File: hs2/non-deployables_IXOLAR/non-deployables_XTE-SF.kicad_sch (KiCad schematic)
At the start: 9 parts, among them J1 Conn_01x01_Pin

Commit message: setting up prototype arrays
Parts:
- removed SC1, SC2, SC3, SC4, SC5, SC6, SC7, SC8: XTE-SF, solar_cells:xte-sf, symbol Device:XTE-SF
- added D1: 1N5400, Diode_THT:D_DO-201AD_P15.24mm_Horizontal, symbol Diode:1N5400
- added SC1, SC10, SC11, SC12, SC13, SC14, SC15, SC16, SC2, SC3, SC4, SC5, SC6, SC7, SC8, SC9: Solar_Cell, solar_cells:XOLAR_SM401K08TF, symbol Device:IXOLAR
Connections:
- net GND: now also SC15.2 (-), SC16.2 (-), SC4.2 (-), SC8.2 (-)
- net at J1.1 (Pin_1): now also D1.1 (K)
- new net: SC5.2 (-), SC6.1 (+)
- new net: SC6.2 (-), SC7.1 (+)
- new net: D1.2 (A), SC1.1 (+), SC10.1 (+), SC5.1 (+), SC9.1 (+)
- new net: SC11.1 (+), SC9.2 (-)
- new net: SC7.2 (-), SC8.1 (+)
- new net: SC14.2 (-), SC16.1 (+)
- new net: SC3.2 (-), SC4.1 (+)
- new net: SC12.2 (-), SC14.1 (+)
- new net: SC11.2 (-), SC13.1 (+)
- new net: SC13.2 (-), SC15.1 (+)
- new net: SC1.2 (-), SC2.1 (+)
- new net: SC10.2 (-), SC12.1 (+)
- new net: SC2.2 (-), SC3.1 (+)
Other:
- moved on the sheet: J1

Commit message: updated schematic
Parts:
- added D2, D3, D4, D5: 1N5400, Diode_THT:D_DO-201AD_P15.24mm_Horizontal, symbol Diode:1N5400
- added J2, Other_Board1, Other_Board2, gnd_connector1: Conn_01x01_Pin, Connector_Wire:SolderWirePad_1x01_SMD_5x10mm, symbol Connector:Conn_01x01_Pin
- added SC17, SC18, SC19, SC20: Solar_Cell, solar_cells:XOLAR_SM401K08TF, symbol Device:IXOLAR
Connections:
- net GND: now also SC19.2 (-), SC20.2 (-), gnd_connector1.1 (Pin_1); no longer SC15.2 (-)
- net at SC9.2 (-): now also SC10.1 (+); no longer SC11.1 (+)
- net at D1.1 (K), J1.1 (Pin_1): now also D2.1 (K), D3.1 (K)
- net at SC16.1 (+): now also SC13.2 (-); no longer SC14.2 (-)
- net at SC12.2 (-): now also SC15.1 (+); no longer SC14.1 (+)
- net at SC11.2 (-): now also SC14.1 (+); no longer SC13.1 (+)
- net at SC12.1 (+): now also D5.2 (A); no longer SC10.2 (-)
- new net: Other_Board1.1 (Pin_1), SC10.2 (-)
- new net: SC14.2 (-), SC17.1 (+)
- new net: SC15.2 (-), SC18.1 (+)
- new net: D3.2 (A), SC9.1 (+)
- new net: D4.1 (K), D5.1 (K), J2.1 (Pin_1)
- new net: D4.2 (A), SC11.1 (+)
- new net: D1.2 (A), SC1.1 (+)
- new net: Other_Board2.1 (Pin_1), SC13.1 (+)
- new net: D2.2 (A), SC5.1 (+)
- new net: SC17.2 (-), SC19.1 (+)
- new net: SC18.2 (-), SC20.1 (+)
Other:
- moved on the sheet: D1, J1, SC1, SC2, SC3, SC4, SC5, SC6, SC7, SC8

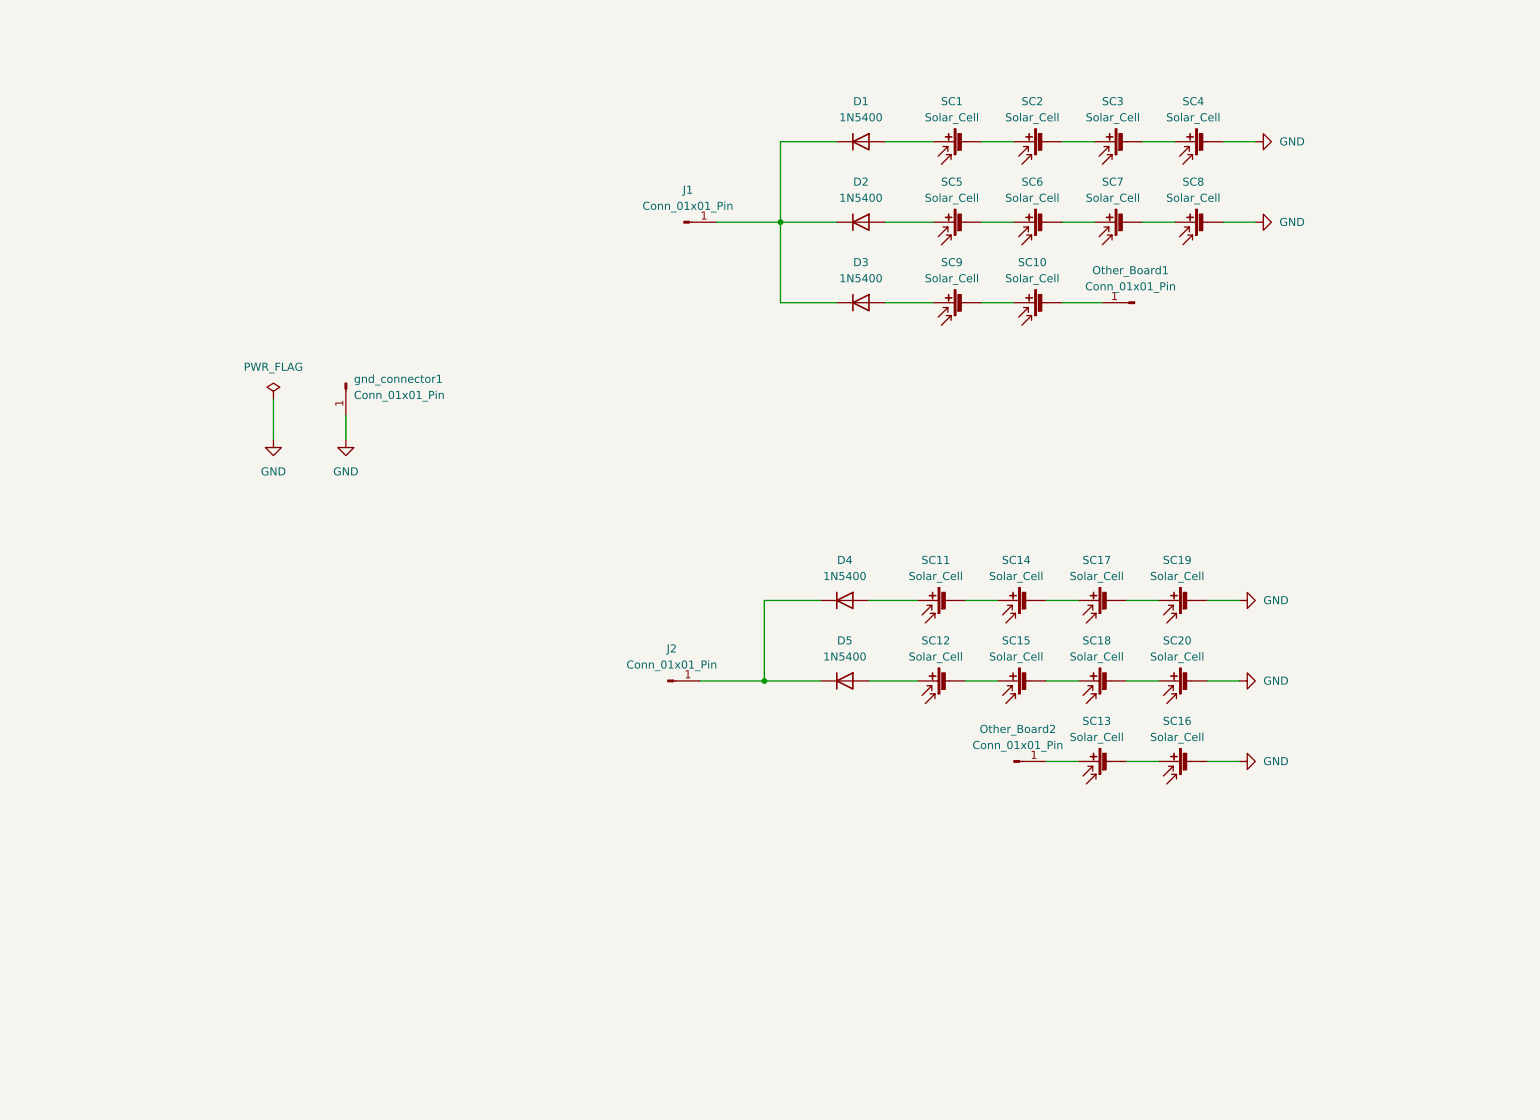
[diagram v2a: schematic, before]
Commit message: started prototype pcbs for 2 panel boards
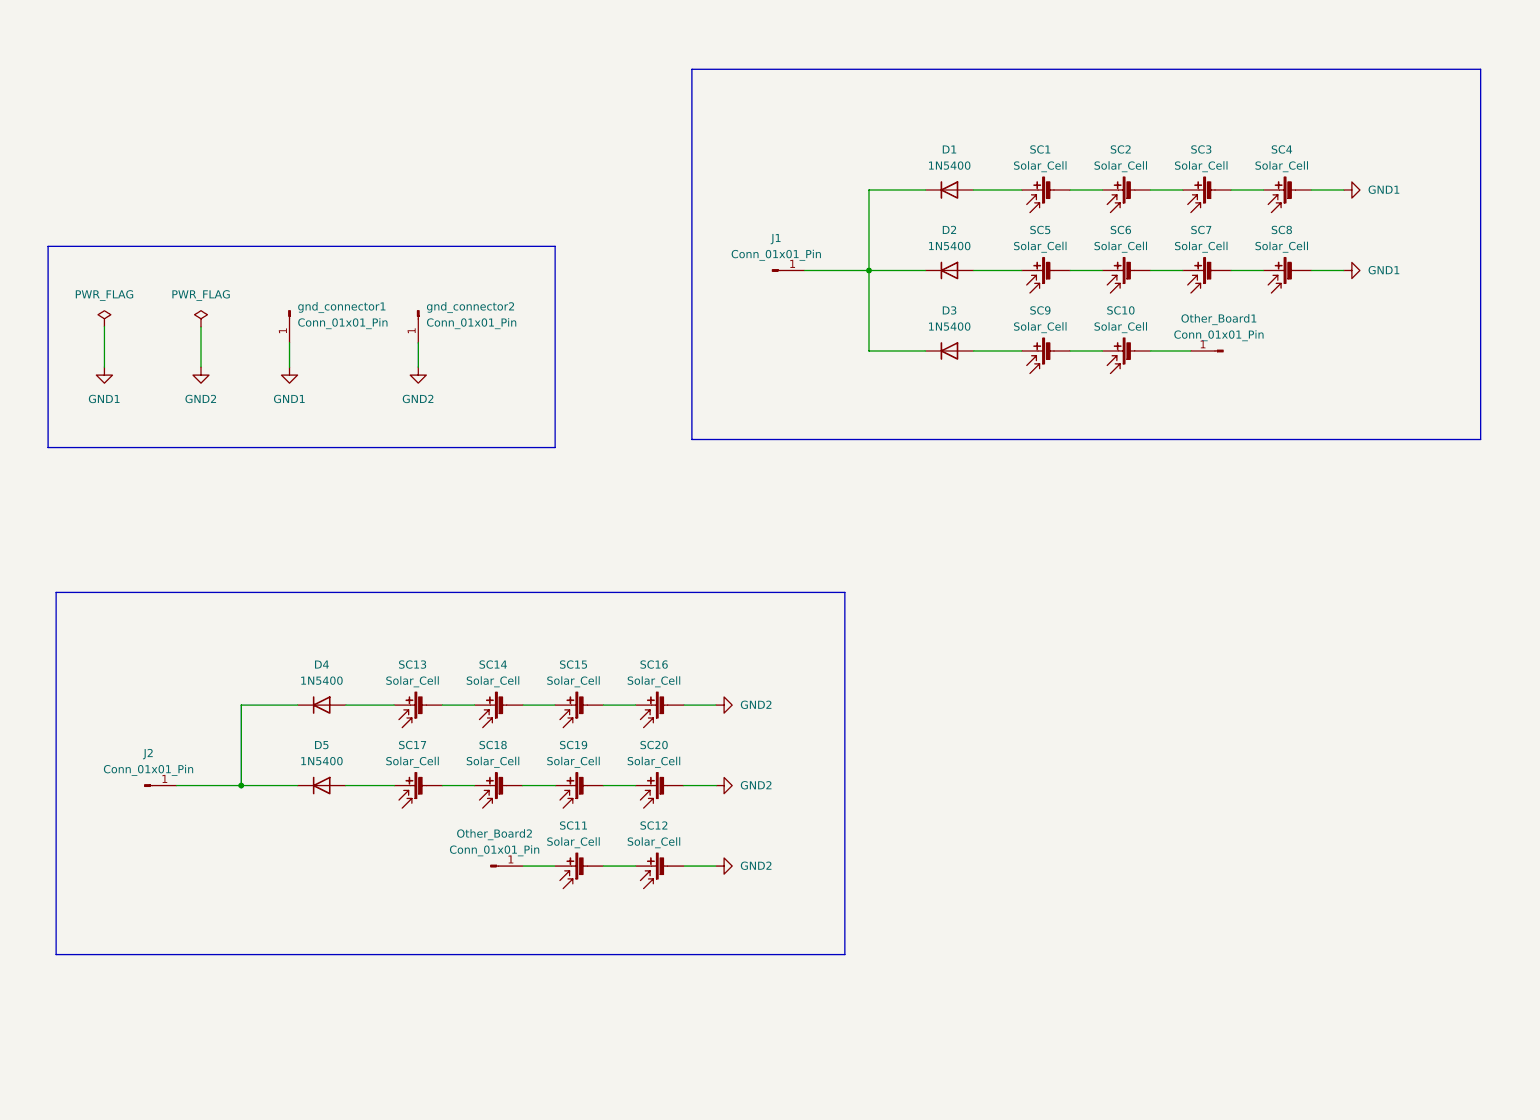
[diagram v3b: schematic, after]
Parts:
- added gnd_connector2: Conn_01x01_Pin, Connector_Wire:SolderWirePad_1x01_SMD_5x10mm, symbol Connector:Conn_01x01_Pin
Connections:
- net at SC13.2 (-): now also SC14.1 (+); no longer SC16.1 (+)
- net at SC12.1 (+): now also SC11.2 (-); no longer D5.2 (A)
- net at SC15.1 (+): now also SC14.2 (-); no longer SC12.2 (-)
- net at SC17.1 (+): now also D5.2 (A); no longer SC14.2 (-)
- net at SC15.2 (-): now also SC16.1 (+); no longer SC18.1 (+)
- net at D4.2 (A): now also SC13.1 (+); no longer SC11.1 (+)
- net at Other_Board2.1 (Pin_1): now also SC11.1 (+); no longer SC13.1 (+)
- net at SC17.2 (-): now also SC18.1 (+); no longer SC19.1 (+)
- net at SC20.1 (+): now also SC19.2 (-); no longer SC18.2 (-)
- net GND renamed GND1
- net GND1: no longer SC16.2 (-), SC19.2 (-), SC20.2 (-)
- new net: SC18.2 (-), SC19.1 (+)
- new net GND2: SC12.2 (-), SC16.2 (-), SC20.2 (-), gnd_connector2.1 (Pin_1)
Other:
- moved on the sheet: D1, D2, D3, D4, D5, J1, J2, Other_Board1, Other_Board2, SC1, SC10, SC12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

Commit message: updated with mounting holes
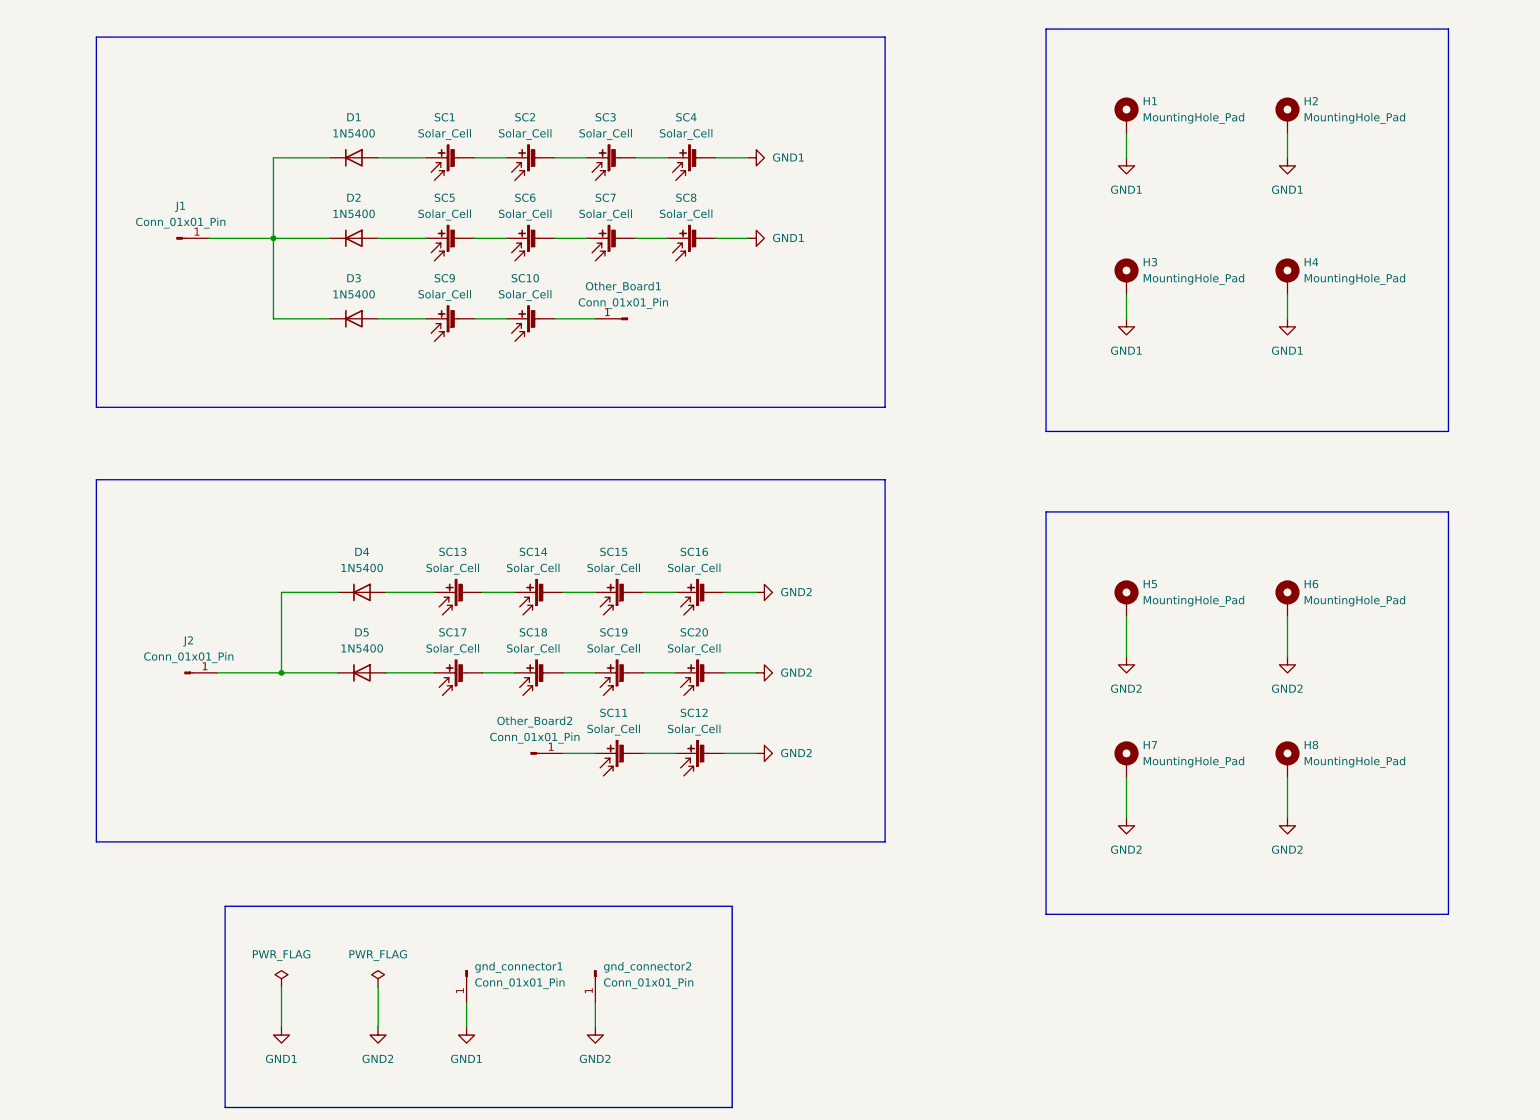
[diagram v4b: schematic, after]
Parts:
- added H1, H2, H3, H4, H5, H6, H7, H8: MountingHole_Pad, MountingHole:MountingHole_3.2mm_M3_DIN965_Pad, symbol Mechanical:MountingHole_Pad
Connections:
- net GND1: now also H1.1, H2.1, H3.1, H4.1
- net GND2: now also H5.1, H6.1, H7.1, H8.1
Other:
- moved on the sheet: D1, D2, D3, D4, D5, J1, J2, Other_Board1, Other_Board2, SC1, SC10, SC11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
